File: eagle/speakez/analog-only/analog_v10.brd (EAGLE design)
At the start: 43.7 x 45.7 mm, 45 parts, among them U1 +12v, U2 MAX5486

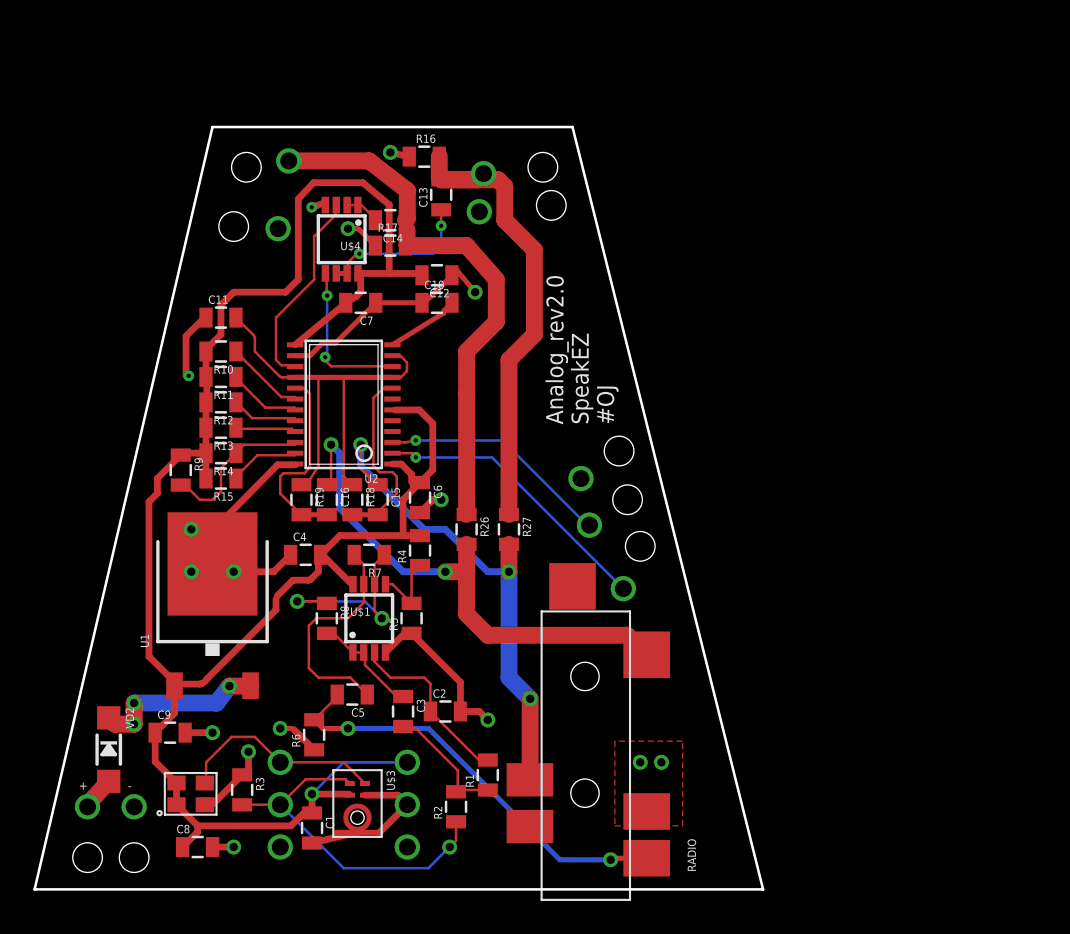
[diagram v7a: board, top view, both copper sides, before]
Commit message: few small tweaks, mostly silkscreen modifications. Added gerbers for pcb order
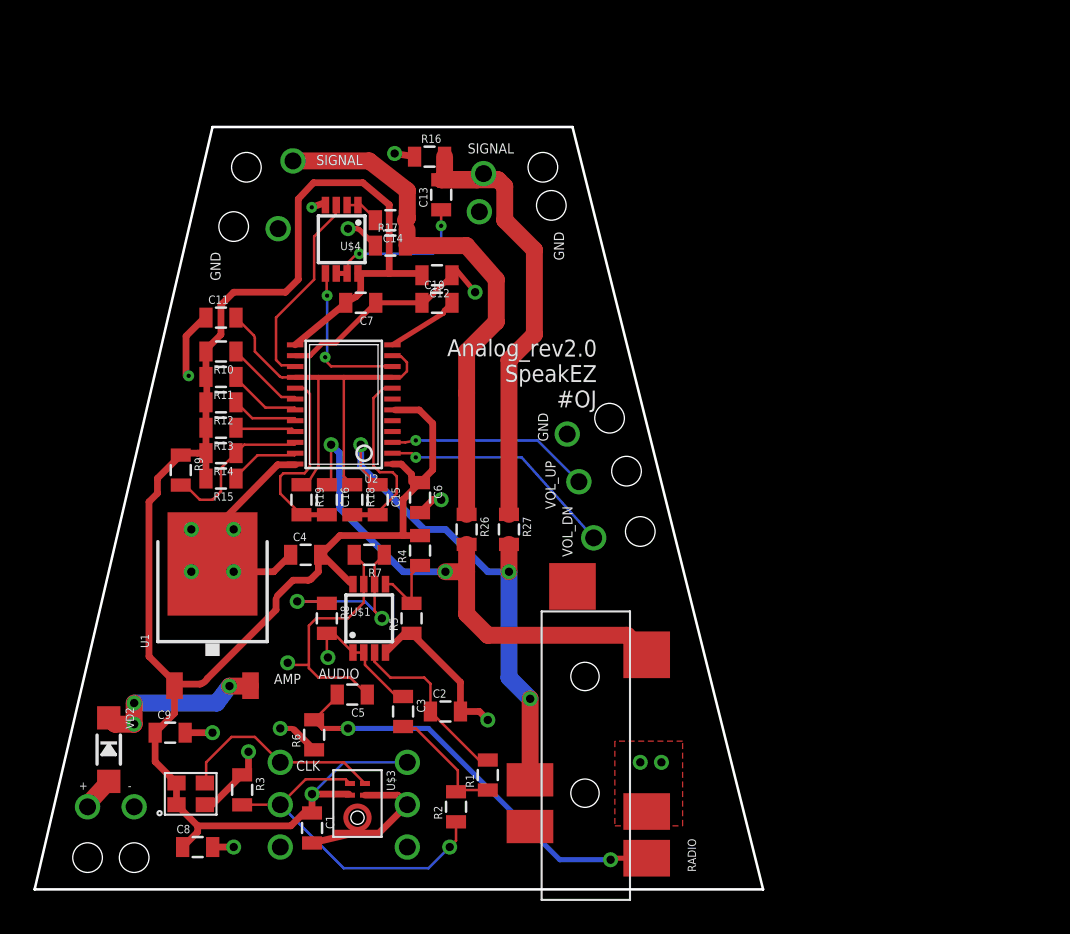
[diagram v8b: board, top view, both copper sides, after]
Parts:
- moved R16 0.32 mm to (21.9, 45.2)
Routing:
- net NO_DN: track 17.2 -> 14.3 mm
- net NO_UP: track 13.9 -> 12.2 mm
- net AUDIO: track 6.54 -> 8.01 mm, vias 0 -> 1
- net VOUT_AMP: track 13.7 -> 15.0 mm, vias 0 -> 1
- net GND: track 69.0 -> 69.1 mm, vias 22 -> 23
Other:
- board text added: "AMP"
- board text added: "AUDIO"
- board text added: "CLK"
- board text added: "GND"
- board text added: "SIGNAL"
- board text added: "VOL_DN"
- board text added: "VOL_UP"
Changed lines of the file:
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@@
 <?xml version="1.0" encoding="utf-8"?>
 <!DOCTYPE eagle SYSTEM "eagle.dtd">
-<eagle version="7.7.0">
+<eagle version="7.6.0">
 <drawing>
 <settings>
@@
 <wire x1="30.48" y1="46.99" x2="8.89" y2="46.99" width="0.1524" layer="20"/>
 <wire x1="8.89" y1="46.99" x2="-1.778" y2="1.27" width="0.1524" layer="20"/>
-<text x="32.96336875" y="29.138103125" size="1.016" layer="21" rot="R89.8">Analog_rev2.0
+<text x="31.948896875" y="34.23336875" size="1.016" layer="21" rot="R179.8">Analog_rev2.0
 SpeakEZ
 #OJ</text>
@@
 <text x="1.397" y="7.747" size="0.5" layer="21" rot="R180">+</text>
 <text x="3.81" y="7.239" size="0.5" layer="21">-</text>
-<hole x="33.274" y="27.559" drill="1.778"/>
-<hole x="33.782" y="24.638" drill="1.778"/>
-<hole x="34.544" y="21.844" drill="1.778"/>
+<hole x="32.7025" y="29.5275" drill="1.778"/>
+<hole x="33.7185" y="26.3525" drill="1.778"/>
+<hole x="34.544" y="22.733" drill="1.778"/>
 <hole x="28.702" y="44.577" drill="1.778"/>
 <hole x="29.21" y="42.291" drill="1.778"/>
 <hole x="10.922" y="44.577" drill="1.778"/>
 <hole x="10.16" y="41.021" drill="1.778"/>
+<text x="30.48" y="21.209" size="0.6096" layer="25" rot="R90">VOL_DN</text>
+<text x="29.464" y="24.0665" size="0.6096" layer="25" rot="R90">VOL_UP</text>
+<text x="29.0195" y="28.1305" size="0.6096" layer="25" rot="R90">GND</text>
+<text x="15.24" y="13.9065" size="0.6096" layer="25">AUDIO</text>
+<text x="12.573" y="13.589" size="0.6096" layer="25">AMP</text>
+<text x="13.9065" y="8.382" size="0.6096" layer="25">CLK</text>
+<text x="29.972" y="38.989" size="0.6096" layer="25" rot="R90">GND</text>
+<text x="8.763" y="39.497" size="0.6096" layer="25" rot="R270">GND</text>
+<text x="24.1935" y="45.4025" size="0.6096" layer="25">SIGNAL</text>
+<text x="15.113" y="44.704" size="0.6096" layer="25">SIGNAL</text>
 </plain>
 <attributes>
@@
 <attribute name="VALUE" x="20.066" y="42.545" size="0.5" layer="27" rot="R180"/>
 </element>
-<element name="R16" library="SparkFun-Resistors" package="0805" value="100k" x="21.59" y="45.212" smashed="yes">
-<attribute name="NAME" x="21.082" y="46.0375" size="0.5" layer="25"/>
-<attribute name="VALUE" x="20.32" y="43.815" size="0.5" layer="27"/>
+<element name="R16" library="SparkFun-Resistors" package="0805" value="100k" x="21.9075" y="45.212" smashed="yes">
+<attribute name="NAME" x="21.3995" y="46.0375" size="0.5" layer="25"/>
+<attribute name="VALUE" x="20.6375" y="43.815" size="0.5" layer="27"/>
 </element>
 <element name="R17" library="SparkFun-Resistors" package="0805" value="100k" x="19.558" y="39.878" smashed="yes">
@@
 <wire x1="17.963" y1="20.761" x2="17.963" y2="19.576" width="0.1524" layer="1"/>
 <wire x1="15.24" y1="13.97" x2="14.6685" y2="14.5415" width="0.1524" layer="1"/>
-<wire x1="14.6685" y1="14.5415" x2="14.6685" y2="17.0815" width="0.1524" layer="1"/>
+<wire x1="14.6685" y1="14.5415" x2="14.6685" y2="14.732" width="0.1524" layer="1"/>
+<wire x1="14.6685" y1="14.732" x2="14.6685" y2="17.0815" width="0.1524" layer="1"/>
 <wire x1="15.24" y1="13.97" x2="17.156" y2="13.97" width="0.1524" layer="1"/>
 <wire x1="17.156" y1="13.97" x2="18.172" y2="12.954" width="0.1524" layer="1"/>
+<via x="13.3985" y="14.859" extent="1-16" drill="0.5"/>
+<wire x1="13.3985" y1="14.859" x2="13.5255" y2="14.732" width="0.1524" layer="1"/>
+<wire x1="13.5255" y1="14.732" x2="14.6685" y2="14.732" width="0.1524" layer="1"/>
 </signal>
 <signal name="N$7">
@@
 <wire x1="18.034" y1="14.732" x2="18.034" y2="15.405" width="0.1524" layer="1"/>
 <wire x1="18.034" y1="15.405" x2="17.963" y2="15.476" width="0.1524" layer="1"/>
+<via x="15.8115" y="15.1765" extent="1-16" drill="0.5"/>
+<wire x1="15.8115" y1="15.1765" x2="15.748" y2="15.24" width="0.1524" layer="1"/>
+<wire x1="15.748" y1="15.24" x2="15.748" y2="16.626" width="0.1524" layer="1"/>
 </signal>
 <signal name="RIGHT">
@@
 <signal name="NO_DN">
 <contactref element="U2" pad="2"/>
-<via x="33.528" y="19.304" extent="1-16" drill="1.016"/>
+<via x="31.75" y="22.352" extent="1-16" drill="1.016"/>
 <via x="21.082" y="27.178" extent="1-16" drill="0.254"/>
 <wire x1="19.6818" y1="27.428" x2="20.832" y2="27.428" width="0.1524" layer="1"/>
 <wire x1="20.832" y1="27.428" x2="21.082" y2="27.178" width="0.1524" layer="1"/>
-<wire x1="21.082" y1="27.178" x2="25.654" y2="27.178" width="0.1524" layer="16"/>
-<wire x1="25.654" y1="27.178" x2="33.528" y2="19.304" width="0.1524" layer="16"/>
+<wire x1="21.082" y1="27.178" x2="27.432" y2="27.178" width="0.1524" layer="16"/>
+<wire x1="31.75" y1="22.352" x2="27.432" y2="27.178" width="0.1524" layer="16"/>
 </signal>
 <signal name="NO_UP">
 <contactref element="U2" pad="3"/>
-<via x="31.496" y="23.114" extent="1-16" drill="1.016"/>
+<via x="30.861" y="25.7175" extent="1-16" drill="1.016"/>
 <via x="21.082" y="28.194" extent="1-16" drill="0.254"/>
 <wire x1="19.6818" y1="28.078" x2="20.458" y2="28.078" width="0.1524" layer="1"/>
 <wire x1="20.458" y1="28.078" x2="21.082" y2="28.194" width="0.1524" layer="1"/>
-<wire x1="31.496" y1="23.114" x2="31.369" y2="23.114" width="0.1524" layer="16"/>
-<wire x1="31.369" y1="23.114" x2="26.289" y2="28.194" width="0.1524" layer="16"/>
-<wire x1="26.289" y1="28.194" x2="21.082" y2="28.194" width="0.1524" layer="16"/>
+<wire x1="30.861" y1="25.7175" x2="28.3845" y2="28.194" width="0.1524" layer="16"/>
+<wire x1="28.3845" y1="28.194" x2="21.082" y2="28.194" width="0.1524" layer="16"/>
 </signal>
 <signal name="NO_MUTE">
@@
 <contactref element="R16" pad="2"/>
 <via x="25.146" y="44.196" extent="1-16" drill="1.016"/>
-<wire x1="22.49" y1="45.212" x2="22.49" y2="43.942" width="1.016" layer="1"/>
-<wire x1="22.49" y1="43.942" x2="22.606" y2="43.826" width="1.016" layer="1"/>
 <wire x1="22.606" y1="43.826" x2="24.776" y2="43.826" width="1.016" layer="1"/>
 <wire x1="24.776" y1="43.826" x2="25.146" y2="44.196" width="1.016" layer="1"/>
@@
 <wire x1="28.194" y1="34.544" x2="26.67" y2="33.02" width="1.016" layer="1"/>
 <wire x1="26.67" y1="33.02" x2="26.67" y2="23.76" width="1.016" layer="1"/>
+<wire x1="22.606" y1="43.826" x2="22.8075" y2="44.0275" width="1.016" layer="1"/>
+<wire x1="22.8075" y1="44.0275" x2="22.8075" y2="45.212" width="1.016" layer="1"/>
 </signal>
 <signal name="HP_L_AMPD">
@@
 <wire x1="20.5606" y1="40.8189" x2="20.458" y2="41.402" width="0.1524" layer="1"/>
 <wire x1="24.13" y1="31.032415625" x2="24.13" y2="31.4457" width="0.4064" layer="1"/>
-<via x="13.462" y="44.958" extent="1-16" drill="1.016"/>
-<wire x1="13.462" y1="44.958" x2="18.288" y2="44.958" width="1.016" layer="1"/>
+<via x="13.716" y="44.958" extent="1-16" drill="1.016"/>
+<wire x1="13.716" y1="44.958" x2="18.288" y2="44.958" width="1.016" layer="1"/>
 <wire x1="18.288" y1="44.958" x2="20.574" y2="43.18" width="1.016" layer="1"/>
 <wire x1="20.574" y1="43.18" x2="20.574" y2="41.518" width="1.016" layer="1"/>
@@
 <wire x1="15.557" y1="42.4272" x2="15.662" y2="42.309" width="0.1524" layer="1"/>
 <via x="14.8422" y="42.1732" extent="1-16" drill="0.254"/>
-<via x="19.558" y="45.466" extent="1-16" drill="0.5"/>
-<wire x1="19.558" y1="45.466" x2="20.69" y2="45.212" width="0.4064" layer="1"/>
+<via x="19.812" y="45.4025" extent="1-16" drill="0.5"/>
+<wire x1="19.812" y1="45.4025" x2="21.0075" y2="45.212" width="0.4064" layer="1"/>
 <via x="17.018" y="40.894" extent="1-16" drill="0.5"/>
 <wire x1="17.018" y1="40.894" x2="17.536790625" y2="40.894" width="0.3048" layer="1"/>
@@
 <wire x1="17.71639375" y1="40.81960625" x2="18.658" y2="39.878" width="0.3048" layer="1"/>
 <wire x1="12.79525" y1="26.7335" x2="13.87475" y2="26.7335" width="0.4064" layer="1"/>
-<wire x1="8.98525" y1="22.86" x2="12.79525" y2="26.7335" width="0.4064" layer="1"/>
 <wire x1="7.62" y1="22.86" x2="8.98525" y2="22.86" width="0.1524" layer="1"/>
 <wire x1="13.87475" y1="26.7335" x2="13.8462" y2="26.778" width="0.1524" layer="1"/>
@@
 <wire x1="13.599790625" y1="10.922" x2="13.77939375" y2="10.84760625" width="0.3048" layer="1" curve="-44.999502"/>
 <wire x1="13.77939375" y1="10.84760625" x2="14.986" y2="9.641" width="0.4064" layer="1"/>
-<via x="30.988" y="25.908" extent="1-16" drill="1.016"/>
+<via x="30.1625" y="28.575" extent="1-16" drill="1.016"/>
 <wire x1="13.8462" y1="33.278" x2="14.228" y2="33.278" width="0.1524" layer="1"/>
 <wire x1="18.796" y1="36.333" x2="18.68" y2="36.449" width="0.1524" layer="1"/>
@@
 <wire x1="15.494" y1="34.036" x2="16.267" y2="34.036" width="0.3048" layer="1"/>
 <wire x1="16.267" y1="34.036" x2="18.68" y2="36.449" width="0.3048" layer="1"/>
+<via x="10.16" y="22.86" extent="1-16" drill="0.5"/>
+<wire x1="8.98525" y1="22.86" x2="12.79525" y2="26.7335" width="0.4064" layer="1"/>
 </signal>
 <signal name="N$17">
